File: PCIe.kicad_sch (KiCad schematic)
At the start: 11 parts, among them J11 1-2199230-5

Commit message: Replace v2 with updated RK3576_SBCv2 (Copy) Oct 2
- Update 18 sheets to Oct 2 15:37 local versions
- Keep cleaned layout: exclude .history/, Resources/, *.bak, *.lck,
  project.kicad_dru, .hs_rules.json, lowercase dup placeholders
  (fixtures/power), empty orphans (digital, mechanical, output,
  USBC_MCU, eMMC_UFS)
- Preserve LICENSE, README.md, .gitignore
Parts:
- R153, R154, R155, R156: LCSC Part C114765 -> C106231; Mouser Part 603-RC0402FR-0722RL -> 603-RC0402FR-070RL
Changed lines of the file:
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@@
 		(polyline
 			(pts
-				(xy 143.1925 40.64) (xy 143.51 68.58) (xy 127.635 68.58) (xy 127.635 40.64)
+				(xy 143.51 40.64) (xy 143.51 68.58) (xy 127.635 68.58) (xy 127.635 40.64)
 			)
 			(stroke
@@
 		)
 		(property "KLC_S4.2_VREG_LX" ""
+			(at 93.98 64.77 0)
+			(hide yes)
+			(show_name no)
+			(do_not_autoplace no)
+			(effects
+				(font
+					(size 1.27 1.27)
+				)
+			)
+		)
+		(property "Sim.Library" ""
 			(at 93.98 64.77 0)
 			(hide yes)
@@
 			)
 		)
+		(property "Sim.Library" ""
+			(at 71.12 67.31 90)
+			(hide yes)
+			(show_name no)
+			(do_not_autoplace no)
+			(effects
+				(font
+					(size 1.27 1.27)
+				)
+			)
+		)
 		(pin "1"
 		)
@@
 			)
 		)
+		(property "Sim.Library" ""
+			(at 71.12 69.85 90)
+			(hide yes)
+			(show_name no)
+			(do_not_autoplace no)
+			(effects
+				(font
+					(size 1.27 1.27)
+				)
+			)
+		)
 		(pin "1"
 		)
@@
 			)
 		)
-		(property "LCSC Part" "C114765"
+		(property "LCSC Part" "C106231"
 			(at 118.11 57.15 90)
 			(hide yes)
@@
 			)
 		)
-		(property "Mouser Part" "603-RC0402FR-0722RL "
+		(property "Mouser Part" "603-RC0402FR-070RL"
+			(at 118.11 57.15 90)
+			(hide yes)
+			(show_name no)
+			(do_not_autoplace no)
+			(effects
+				(font
+					(size 1.27 1.27)
+				)
+			)
+		)
+		(property "Sim.Library" ""
 			(at 118.11 57.15 90)
 			(hide yes)
@@
 			)
 		)
+		(property "Sim.Library" ""
+			(at 146.05 52.07 0)
+			(hide yes)
+			(show_name no)
+			(do_not_autoplace no)
+			(effects
+				(font
+					(size 1.27 1.27)
+				)
+			)
+		)
 		(pin "1"
 		)
@@
 			)
 		)
+		(property "Sim.Library" ""
+			(at 45.72 41.91 0)
+			(hide yes)
+			(show_name no)
+			(do_not_autoplace no)
+			(effects
+				(font
+					(size 1.27 1.27)
+				)
+			)
+		)
 		(pin "1"
 		)
@@
 			)
 		)
-		(property "LCSC Part" "C114765"
+		(property "LCSC Part" "C106231"
 			(at 118.11 59.69 90)
 			(hide yes)
@@
 			)
 		)
-		(property "Mouser Part" "603-RC0402FR-0722RL "
+		(property "Mouser Part" "603-RC0402FR-070RL"
+			(at 118.11 59.69 90)
+			(hide yes)
+			(show_name no)
+			(do_not_autoplace no)
+			(effects
+				(font
+					(size 1.27 1.27)
+				)
+			)
+		)
+		(property "Sim.Library" ""
 			(at 118.11 59.69 90)
 			(hide yes)
@@
 			)
 		)
-		(property "LCSC Part" "C114765"
+		(property "LCSC Part" "C106231"
 			(at 118.11 67.31 90)
 			(hide yes)
@@
 			)
 		)
-		(property "Mouser Part" "603-RC0402FR-0722RL "
+		(property "Mouser Part" "603-RC0402FR-070RL"
+			(at 118.11 67.31 90)
+			(hide yes)
+			(show_name no)
+			(do_not_autoplace no)
+			(effects
+				(font
+					(size 1.27 1.27)
+				)
+			)
+		)
+		(property "Sim.Library" ""
 			(at 118.11 67.31 90)
 			(hide yes)
@@
 			)
 		)
+		(property "Sim.Library" ""
+			(at 36.83 41.91 0)
+			(hide yes)
+			(show_name no)
+			(do_not_autoplace no)
+			(effects
+				(font
+					(size 1.27 1.27)
+				)
+			)
+		)
 		(pin "1"
 		)
@@
 			)
 		)
-		(property "LCSC Part" "C114765"
+		(property "LCSC Part" "C106231"
 			(at 118.11 62.23 90)
 			(hide yes)
@@
 			)
 		)
-		(property "Mouser Part" "603-RC0402FR-0722RL "
+		(property "Mouser Part" "603-RC0402FR-070RL"
+			(at 118.11 62.23 90)
+			(hide yes)
+			(show_name no)
+			(do_not_autoplace no)
+			(effects
+				(font
+					(size 1.27 1.27)
+				)
+			)
+		)
+		(property "Sim.Library" ""
 			(at 118.11 62.23 90)
 			(hide yes)
@@
 			(at 154.94 52.07 0)
 			(hide yes)
+			(show_name no)
+			(do_not_autoplace no)
+			(effects
+				(font
+					(size 1.27 1.27)
+				)
+			)
+		)
+		(property "Sim.Library" ""
+			(at 154.94 52.07 0)
+			(hide yes)

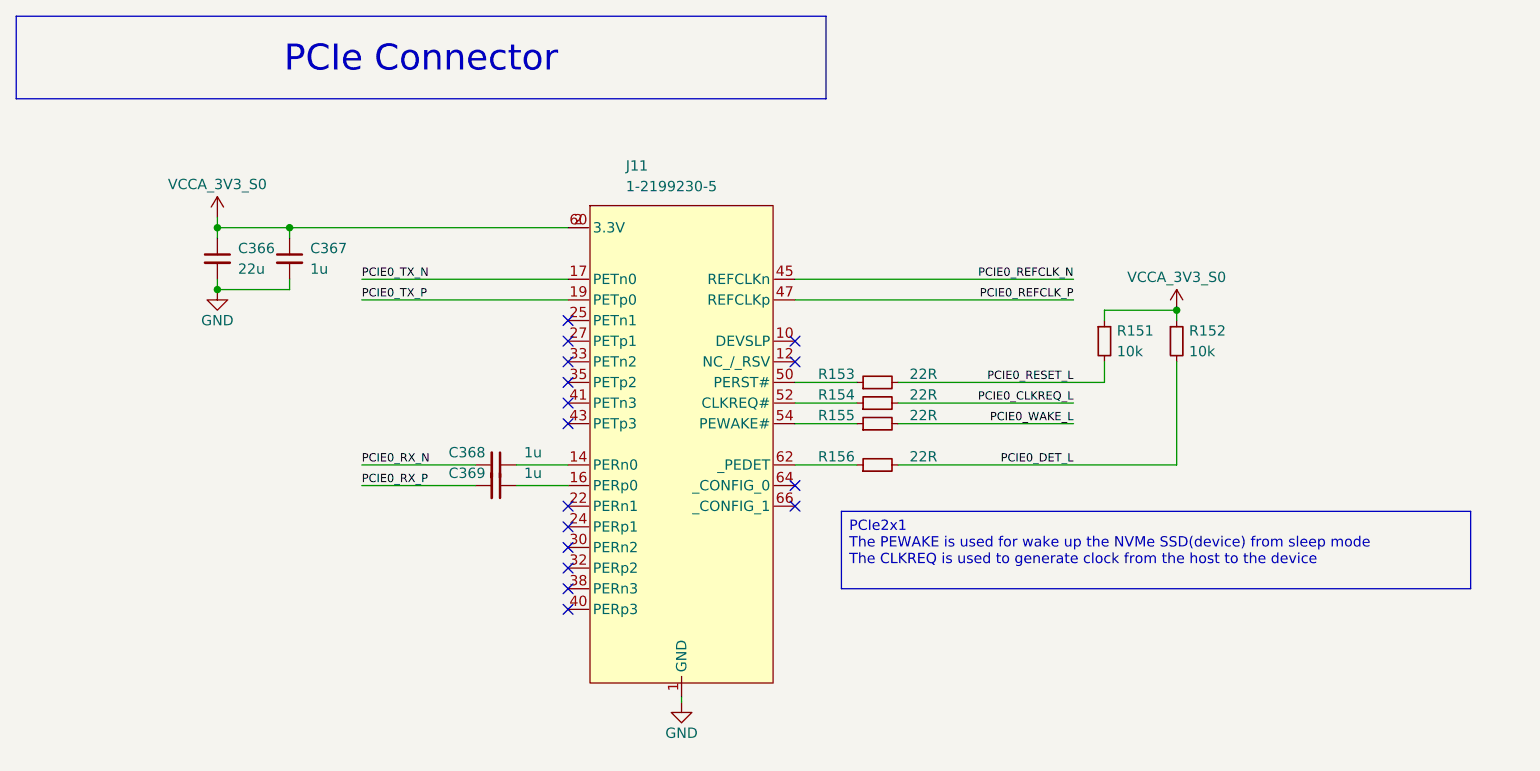
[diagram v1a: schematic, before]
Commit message: Relink hierarchical root: 18 sheets into RK3576 SBCv2 top level
Root was empty (no sheet boxes); all subsheets orphaned.
Rebuilt A1 top level linking RK3576, LPDDR5, Power, Ethernet,
HDMI, MIPI, PCIe, USB-A/C, Wireless, RTC, uSD, GPIO, OLED,
RP2350A, Connectors, Fixtures, DC_Power. block_diagrame kept
docs-only (unlinked, avoids double-instantiation). Lowercase
stub duplicates excluded. ERC: 1388 -> 770 violations.
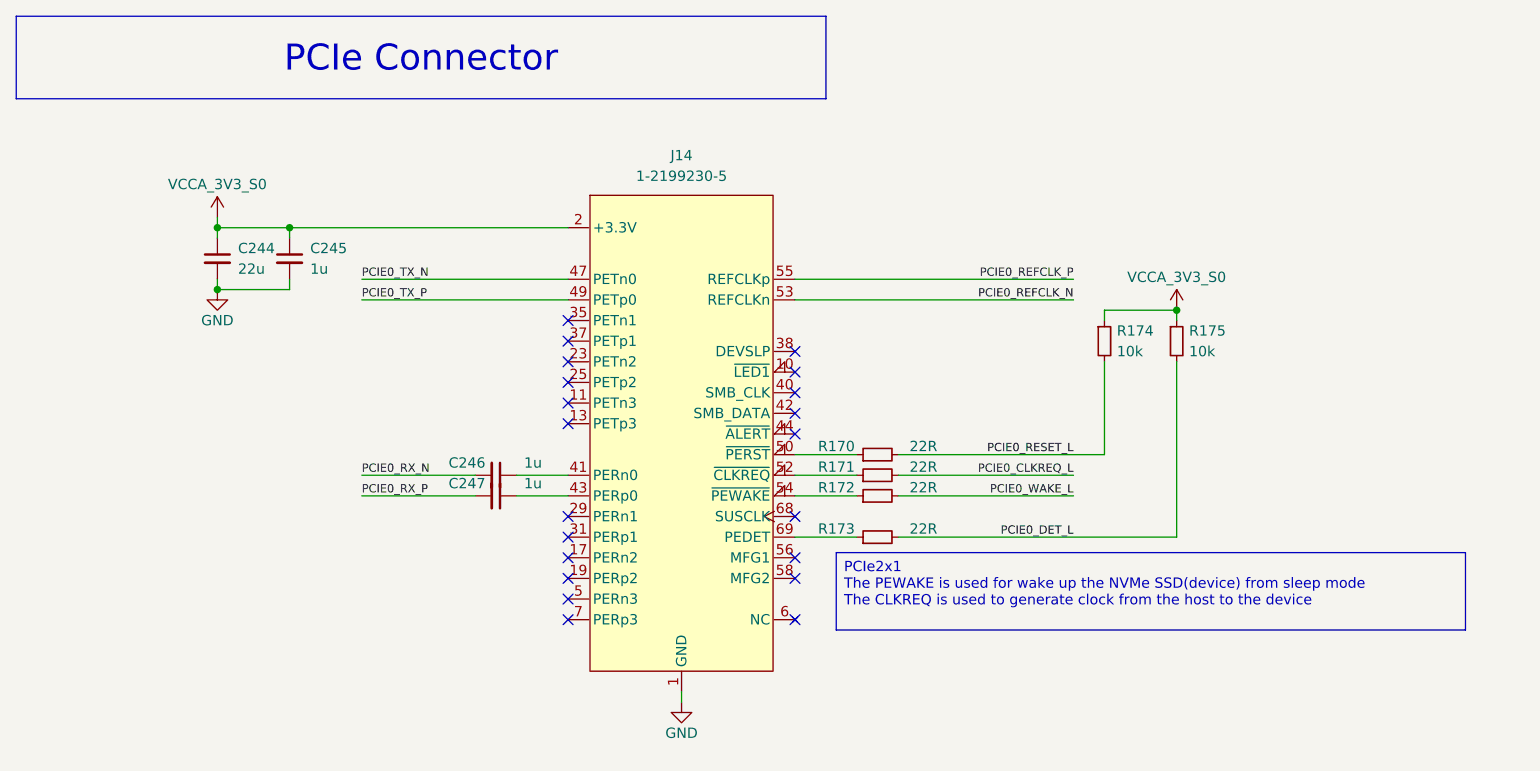
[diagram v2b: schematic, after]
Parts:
- removed J11: 1-2199230-5, easyeda2kicad:PCIE-SMD_75P-P0.50_1-2199230-5, symbol easyeda2kicad:1-2199230-5
- added J14: 1-2199230-5, easyeda2kicad:PCIE-SMD_75P-P0.50_1-2199230-5, symbol easyeda2kicad:1-2199230-5
- renumbered C366 to C244, C367 to C245, C368 to C246, C369 to C247, R153 to R170, R154 to R171, R155 to R172, R156 to R173, R151 to R174, R152 to R175
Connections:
- net GND: now also J14.1 (GND), J14.15 (GND), J14.21 (GND), J14.27 (GND), J14.3 (GND), J14.33 (GND), J14.39 (GND), J14.45 (GND), J14.51 (GND), J14.57 (GND), J14.71 (GND), J14.73 (GND), J14.75 (GND), J14.9 (GND)
- net PCIE0_REFCLK_N: now also J14.53 (REFCLKn)
- net PCIE0_REFCLK_P: now also J14.55 (REFCLKp)
- net PCIE0_TX_N: now also J14.47 (PETn0)
- net PCIE0_TX_P: now also J14.49 (PETp0)
- net at C246.1: now also J14.41 (PERn0)
- net at C247.1: now also J14.43 (PERp0)
- net at R170.1: now also J14.50 (~{PERST})
- net at R171.1: now also J14.52 (~{CLKREQ})
- net at R172.1: now also J14.54 (~{PEWAKE})
- net at R173.1: now also J14.69 (PEDET)
- net VCCA_3V3_S0 renamed +3.3V
- net +3.3V: now also J14.12 (+3.3V), J14.14 (+3.3V), J14.16 (+3.3V), J14.18 (+3.3V), J14.2 (+3.3V), J14.4 (+3.3V), J14.70 (+3.3V), J14.72 (+3.3V), J14.74 (+3.3V)
- new net: J14.20 (NC), J14.22 (NC), J14.24 (NC), J14.26 (NC), J14.28 (NC), J14.30 (NC), J14.32 (NC), J14.34 (NC), J14.36 (NC), J14.46 (NC), J14.48 (NC), J14.6 (NC), J14.67 (NC), J14.8 (NC)
- no-connect marks 16 -> 21
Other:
- moved on the sheet: C246, C247, R170, R171, R172, R173

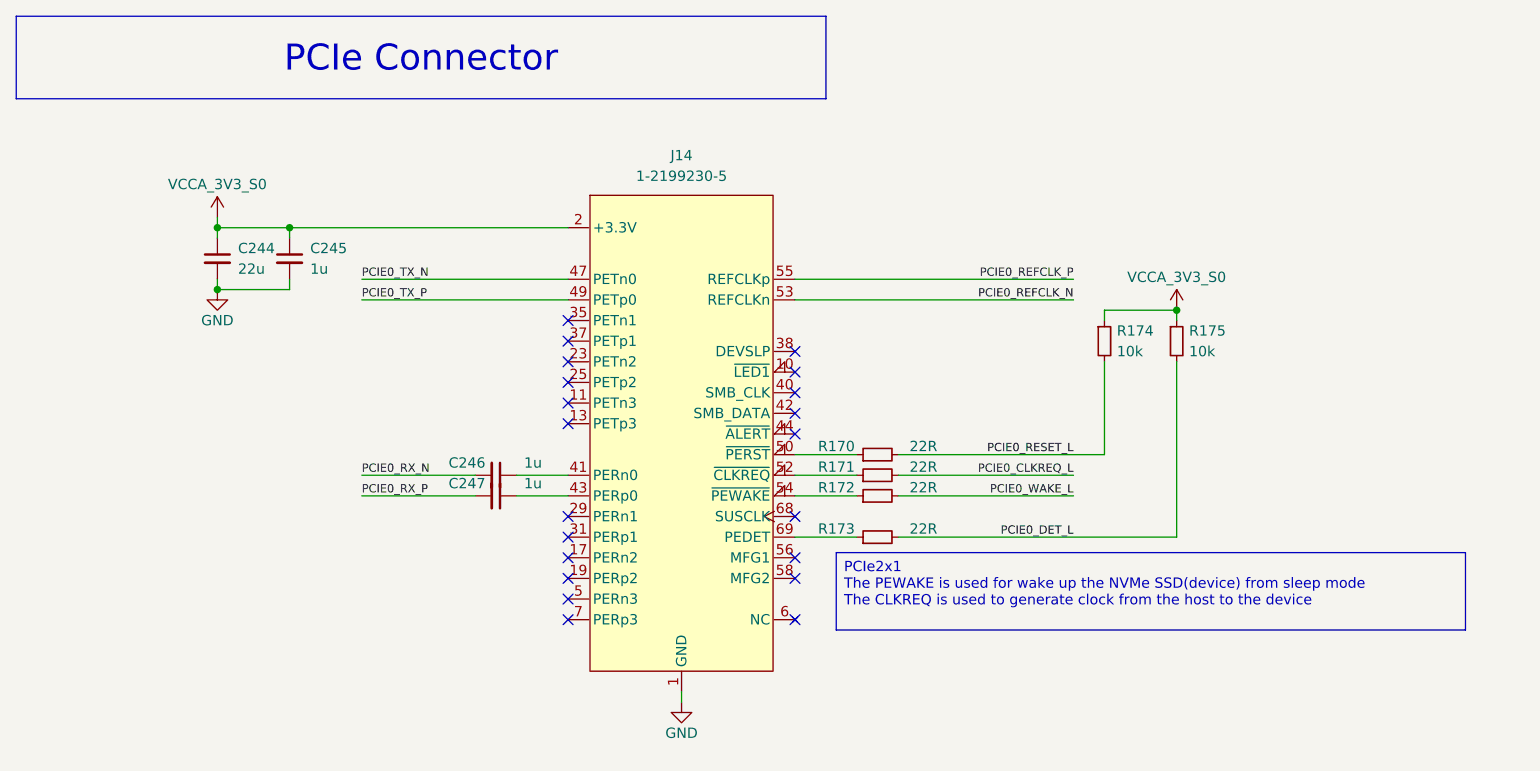
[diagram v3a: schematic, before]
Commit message: block diagrame with Hierarchical labels and NVMe SSD footprint
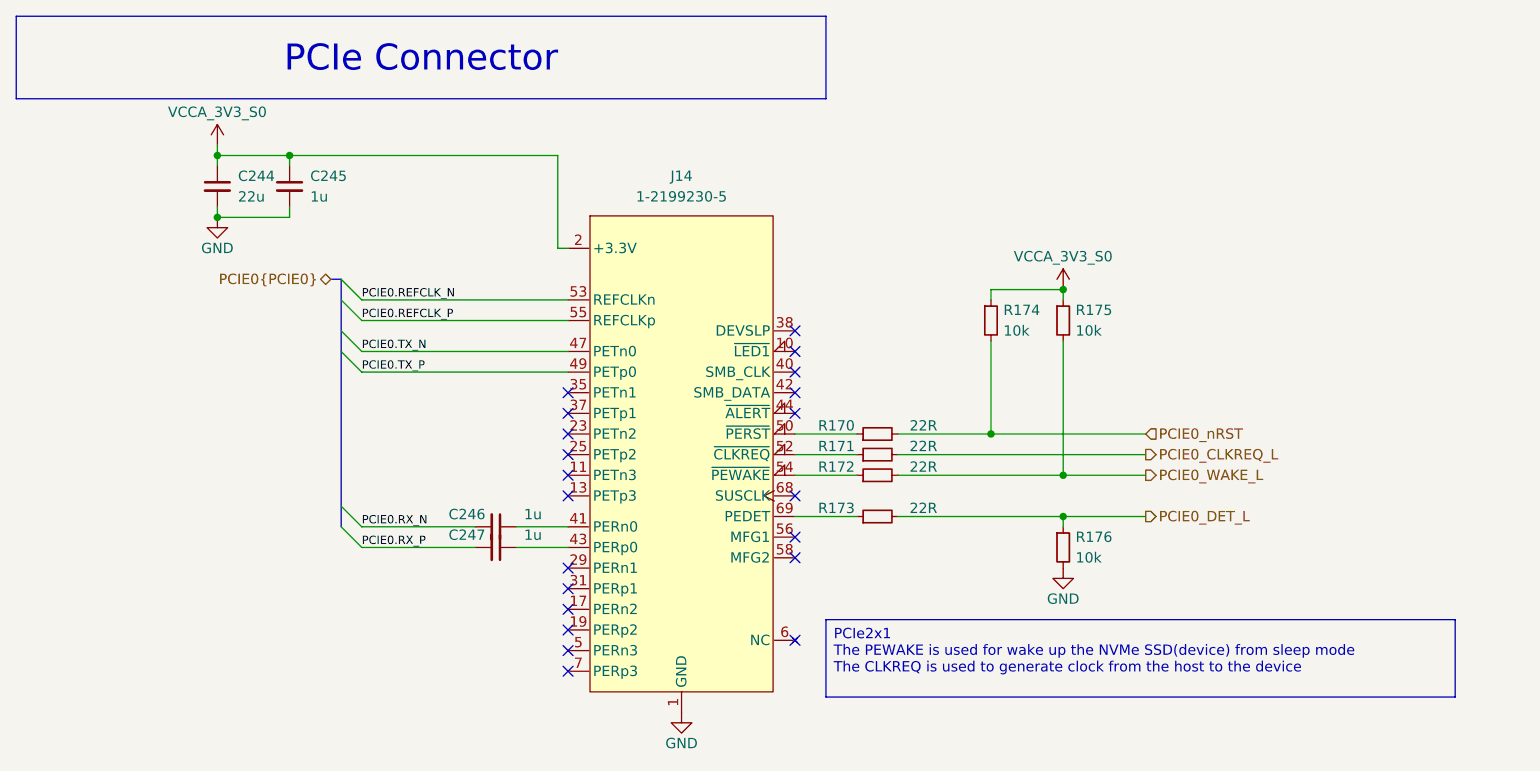
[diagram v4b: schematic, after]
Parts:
- added R176: 10k, PCM_Resistor_SMD_AKL:R_0402_1005Metric, symbol Device:R_Small
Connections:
- net GND: now also R176.2
- net PCIE0_DET_L: now also R176.1; no longer R175.2
- net PCIE0_WAKE_L: now also R175.2
- net PCIE0_REFCLK_N renamed PCIE0.REFCLK_N
- net PCIE0_REFCLK_P renamed PCIE0.REFCLK_P
- net PCIE0_RESET_L renamed PCIE0_nRST
- net PCIE0_RX_N renamed PCIE0.RX_N
- net PCIE0_RX_P renamed PCIE0.RX_P
- net PCIE0_TX_N renamed PCIE0.TX_N
- net PCIE0_TX_P renamed PCIE0.TX_P
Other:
- moved on the sheet: C244, C245, C246, C247, J14, R170, R171, R172, R173, R174, R175
